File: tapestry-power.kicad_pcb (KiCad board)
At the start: 2 copper layers, 76.2 x 25.4 mm, 22 parts, among them J2 4.5-20V, J3 5V, J4 4.5-20V, J5 5V, U1 sic450

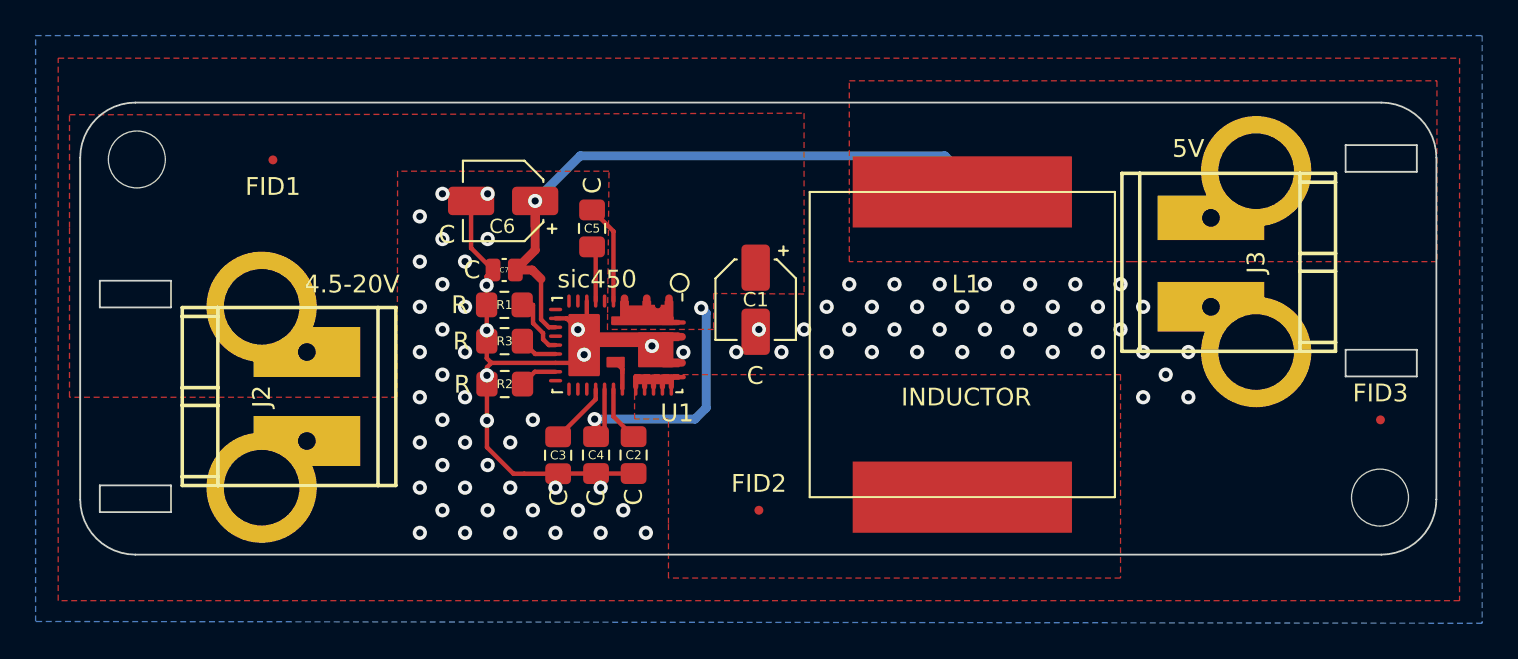
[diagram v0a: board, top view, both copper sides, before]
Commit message: Updated board to wire in enable pin
And included some relevant resistor and capacitor values.
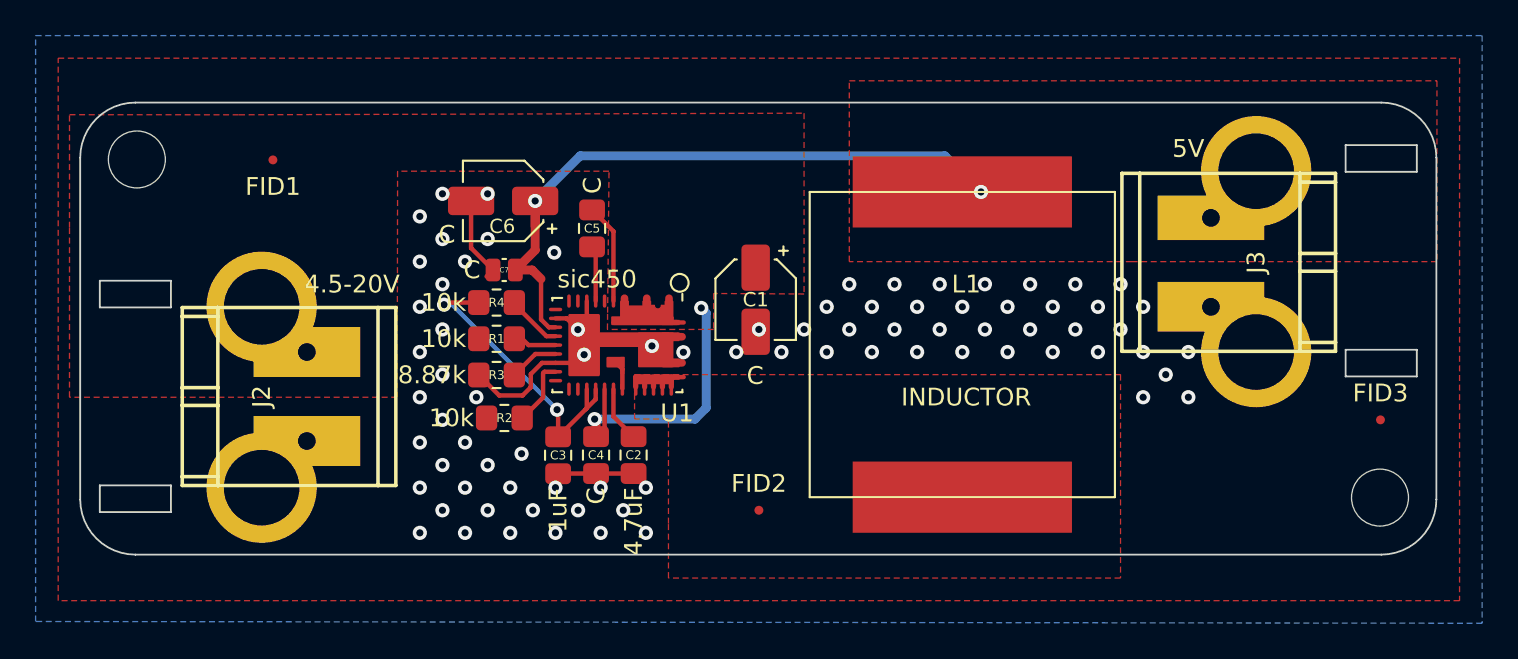
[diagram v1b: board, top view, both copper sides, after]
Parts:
- added R4: 10k, Resistor_SMD:R_0805_2012Metric_Pad1.20x1.40mm_HandSolder, F.Cu at (127.5, 62.0)
- C2: value C -> 4.7uF
- C3: value C -> 1uF
- R1, R2: value R -> 10k
- R3: value R -> 8.87k
- moved R1 1.96 mm to (127.5, 64.0)
- moved R3 1.95 mm to (127.5, 66.1)
- moved R2 1.91 mm to (127.9, 68.5)
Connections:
- C3 pad 1: Net-(C3-Pad1) -> /ENABLE
- U1 pad 22: Net-(C3-Pad1) -> /ENABLE
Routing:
- net /ENABLE: track 0.00 -> 17.0 mm, vias 0 -> 2
- net GND: track 36.5 -> 24.9 mm, vias 85 -> 80
- net Net-(C3-Pad1): track 3.55 -> 0.00 mm
- net /Pgood: track 0.00 -> 3.15 mm
- net Net-(R2-Pad1): track 2.14 -> 3.73 mm
- net Net-(R1-Pad1): track 3.61 -> 2.02 mm
- net Net-(R3-Pad1): track 2.16 -> 2.80 mm
- net /VOUT: vias 1 -> 2
